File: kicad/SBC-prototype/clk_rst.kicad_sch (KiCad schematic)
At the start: 3 parts, among them IC1 DS1813R-10+T&R, SW1 Reset, Y1 ECS-2100AX-1.0MHZ

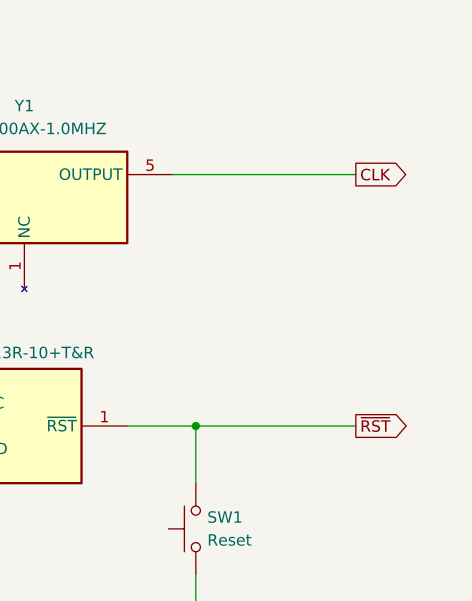
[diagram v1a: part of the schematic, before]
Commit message: Started including hierarchical flow in the top level sheet
- First, hierarchical designs - I don't need a schematic to all fit on
  one sheet.
- I had the clock and reset lines as global labels, so I converted them
  to hierarchical labels instead, imported them on each sheet, and then
  connected the sheets together. It probably looks like overkill right
  now, but it will allow me to modify each block more easily
- The VIA has unconnected ports for now because I haven't wired them to
  anything on the prototyep in the lab yet. That's next, once the
  EEPROM, SRAM, and address decoders are all working (and VIA1 doesn't
  need a load except for maybe some resistors for now).
- Finally, the power rails and ground are global labels right now and
  aren't connected to anything on the top level design schematic. I'm
  not sure if that's normal, so for now I've just left them.
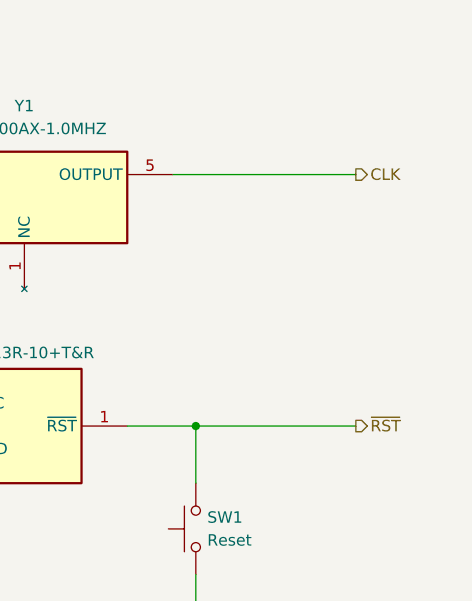
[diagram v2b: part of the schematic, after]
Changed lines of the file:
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@@
 	(title_block
 		(title "65C02 Single Board Computer")
-		(rev "Mk. 0")
+		(rev "Proto")
 	)
 	(junction
@@
 		)
 	)
-	(global_label "~{RST}"
+	(hierarchical_label "CLK"
+		(shape output)
+		(at 168.91 78.74 0)
+		(fields_autoplaced yes)
+		(effects
+			(font
+				(size 1.27 1.27)
+			)
+			(justify left)
+		)
+	)
+	(hierarchical_label "~{RST}"
 		(shape output)
 		(at 168.91 106.68 0)
@@
 			(justify left)
 		)
-		(property "Intersheetrefs" "${INTERSHEET_REFS}"
-			(at 175.3423 106.68 0)
-			(effects
-				(font
-					(size 1.27 1.27)
-				)
-				(justify left)
-				(hide yes)
-			)
-		)
 	)
-	(global_label "CLK"
-		(shape output)
-		(at 168.91 78.74 0)
-		(fields_autoplaced yes)
-		(effects
-			(font
-				(size 1.27 1.27)
-			)
-			(justify left)
-		)
-		(property "Intersheetrefs" "${INTERSHEET_REFS}"
-			(at 175.4633 78.74 0)
-			(effects
-				(font
-					(size 1.27 1.27)
-				)
-				(justify left)
-				(hide yes)
-			)
-		)
-	)
